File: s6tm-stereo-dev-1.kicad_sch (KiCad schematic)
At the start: 86 parts, among them J10 Conn_01x04_Pin, J2 Micro_SD_Card_Det1, J3 USB_C_Receptacle_USB2.0_14P, SW1 SW_SPDT, SW10 SW_Push, SW2 RotaryEncoder_Switch, SW5 SW_Push, SW6 SW_Push, SW7 SW_Push, SW9 SW_Push, U10 HS96L03W2C03, U4 ESP32-S3FN8, Y1 48M

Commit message: schem: add missing footprints
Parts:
- J2: footprint Pers:microSD_Hanbo_TF012 -> GLCS:microSD_Hanbo_TF012
- SW2: footprint RotaryEncoder_Alps_EC11E-Switch_Vertical_H20mm -> Rotary_Encoder:RotaryEncoder_Alps_EC11E-Switch_Vertical_H20mm
- U10: footprint Pers:HS96L03W2C03 -> GLCS:HS96L03W2C03
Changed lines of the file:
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@@
 			)
 		)
-		(property "Footprint" "Pers:microSD_Hanbo_TF012"
+		(property "Footprint" "GLCS:microSD_Hanbo_TF012"
 			(at 144.78 153.67 0)
 			(hide yes)
@@
 			)
 		)
-		(property "Footprint" "RotaryEncoder_Alps_EC11E-Switch_Vertical_H20mm"
+		(property "Footprint" "Rotary_Encoder:RotaryEncoder_Alps_EC11E-Switch_Vertical_H20mm"
 			(at 257.81 31.496 0)
 			(hide yes)
@@
 			)
 		)
-		(property "Footprint" "Pers:HS96L03W2C03"
+		(property "Footprint" "GLCS:HS96L03W2C03"
 			(at 260.35 55.245 0)
 			(hide yes)

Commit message: schem: run and fix ERC
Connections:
- net CHIP_PU: now also C14.1, R14.2, U4.4 (CHIP_PU/RESET)
- no-connect marks 9 -> 13
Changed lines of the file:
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@@
 	)
 	(junction
+		(at 254 153.67)
+		(diameter 0)
+		(color 0 0 0 0)
+	)
+	(junction
 		(at 195.58 119.38)
 		(diameter 0)
@@
 	)
 	(no_connect
+		(at 127 123.19)
+	)
+	(no_connect
 		(at 60.96 107.95)
 	)
 	(no_connect
+		(at 127 120.65)
+	)
+	(no_connect
 		(at 127 74.93)
 	)
 	(no_connect
+		(at 127 115.57)
+	)
+	(no_connect
 		(at 60.96 105.41)
 	)
@@
 	)
 	(no_connect
+		(at 127 118.11)
+	)
+	(no_connect
 		(at 60.96 102.87)
 	)
@@
 	(wire
 		(pts
-			(xy 251.46 153.67) (xy 255.27 153.67)
+			(xy 251.46 153.67) (xy 254 153.67)
 		)
 		(stroke
@@
 	(wire
 		(pts
+			(xy 254 153.67) (xy 255.27 153.67)
+		)
+		(stroke
+			(width 0)
+			(type default)
+		)
+	)
+	(wire
+		(pts
 			(xy 252.73 142.24) (xy 250.19 142.24)
 		)
@@
 		)
 	)
+	(label "CHIP_PU"
+		(at 59.69 64.77 180)
+		(effects
+			(font
+				(size 1.27 1.27)
+			)
+			(justify right bottom)
+		)
+	)
 	(label "DIN"
 		(at 134.62 85.09 180)
@@
 		(property "Value" "GND"
 			(at 60.706 189.738 0)
+			(hide yes)
 			(show_name no)
 			(do_not_autoplace no)
@@
 		(property "Value" "GND"
 			(at 45.212 189.738 0)
+			(hide yes)
 			(show_name no)
 			(do_not_autoplace no)
@@
 					(unit 1)
 				)
+			)
+		)
+	)
+	(symbol
+		(lib_id "power:PWR_FLAG")
+		(at 254 153.67 0)
+		(unit 1)
+		(body_style 1)
+		(exclude_from_sim no)
+		(in_bom yes)
+		(on_board yes)
+		(in_pos_files yes)
+		(dnp no)
+		(fields_autoplaced yes)
+		(property "Reference" "#FLG07"
+			(at 254 151.765 0)
+			(hide yes)
+			(show_name no)
+			(do_not_autoplace no)
+			(effects
+				(font
+					(size 1.27 1.27)
+				)
+			)
+		)
+		(property "Value" "PWR_FLAG"
+			(at 254 148.59 0)
+			(hide yes)
+			(show_name no)
+			(do_not_autoplace no)
+			(effects
+				(font
+					(size 1.27 1.27)
+				)
+			)
+		)
+		(property "Footprint" ""
+			(at 254 153.67 0)
+			(hide yes)
+			(show_name no)
+			(do_not_autoplace no)
+			(effects
+				(font
+					(size 1.27 1.27)
+				)
+			)
+		)
+		(property "Datasheet" ""
+			(at 254 153.67 0)
+			(hide yes)
+			(show_name no)
+			(do_not_autoplace no)
+			(effects
+				(font
+					(size 1.27 1.27)
+				)
+			)
+		)
+		(property "Description" "Special symbol for telling ERC where power comes from"
+			(at 254 153.67 0)
+			(hide yes)
+			(show_name no)
+			(do_not_autoplace no)
+			(effects
+				(font
+					(size 1.27 1.27)
+				)
+			)
+		)
+		(pin "1"
+		)
+		(instances
+			(project "s6tm-stereo-dev-1"
+				(path "/41fad0d7-0cae-453e-a16c-bdf8be036e99"
+					(reference "#FLG07")
+					(unit 1)
+				)

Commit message: schem: add title
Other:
- company: (none) -> Rémi Ait-Younes
- title: (none) -> S6TM Stereo Dev 1
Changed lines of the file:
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@@
 	(generator_version "10.0")
 	(paper "A4")
+	(title_block
+		(title "S6TM Stereo Dev 1")
+		(date "2026-04-11")
+		(rev "01")
+		(company "Rémi Ait-Younes")
+	)
 	(rectangle
 		(start 180.34 138.43)

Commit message: schem: reannotate
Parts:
- renumbered C12 to C1, C20 to C10, C21 to C11, C7 to C12, C8 to C13, C62 to C14, C4 to C2, C13 to C3, C14 to C4, C15 to C5, C16 to C6, C17 to C7, C18 to C8, C19 to C9, D17 to D1, D5 to D10, D12 to D2, D13 to D3, D14 to D4, D15 to D5, D1 to D6, D16 to D7, D2 to D8, D4 to D9, J2 to J1, J10 to J2, L2 to L1, L3 to L2, L4 to L3, L5 to L4, L1 to L5, R11 to R1, R47 to R10, R48 to R11, R49 to R12, R43 to R13, R42 to R14, R16 to R15, R17 to R16, R41 to R17, R14 to R2, R40 to R20, R38 to R21, R39 to R22, R32 to R23, R33 to R24, R34 to R25, R1 to R26, R2 to R27, R35 to R28, R36 to R29, R61 to R3, R37 to R30, R52 to R4, R51 to R5, R50 to R6, R44 to R7, R45 to R8, R46 to R9, SW5 to SW2, SW6 to SW3, SW7 to SW4, SW9 to SW5, SW10 to SW6, SW2 to SW7, TP20 to TP1, TP8 to TP12, TP19 to TP2, TP18 to TP3, TP17 to TP4, TP16 to TP5, TP15 to TP6, TP14 to TP7, TP13 to TP8, TP12 to TP9, U4 to U1, U10 to U2

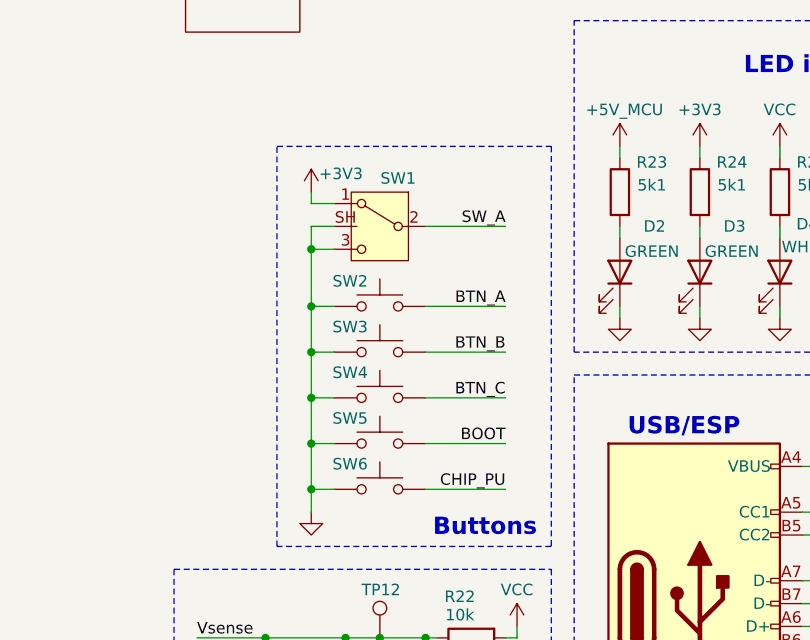
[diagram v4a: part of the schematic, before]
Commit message: schem: remove BTN_C
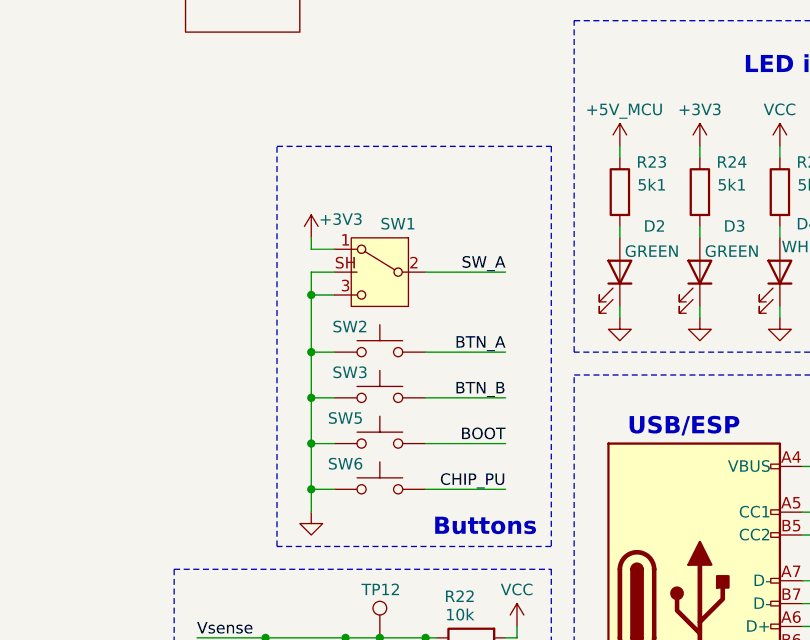
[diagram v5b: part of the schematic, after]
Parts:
- removed SW4: SW_Push, Button_Switch_THT:SW_SPST_Omron_B3F-40xx, symbol Switch:SW_Push
- SW5, SW6: footprint Button_Switch_THT:SW_SPST_Omron_B3F-40xx -> Button_Switch_SMD:SW_SPST_TS-1088-xR020; Basic Z -> Y; JLCPCB Part # C84931 -> C720477; Manufacturer OMRON -> XUNPU; Manufacturer Part Number B3F-4055 -> TS-1088-AR02016
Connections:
- net BOOT: now also SW5.2; no longer SW5.1
- net CHIP_PU: now also SW6.2; no longer SW6.1
- net GND: now also SW5.1, SW6.1; no longer SW5.2, SW6.2
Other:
- moved on the sheet: SW1, SW2, SW3

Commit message: schem: update esp32s3 footprint
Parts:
- U1: footprint Package_DFN_QFN:QFN-56-1EP_7x7mm_P0.4mm_EP5.6x5.6mm -> Package_DFN_QFN:QFN-56-1EP_7x7mm_P0.4mm_EP4x4mm_ThermalVias
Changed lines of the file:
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@@
 			)
 		)
-		(property "Footprint" "Package_DFN_QFN:QFN-56-1EP_7x7mm_P0.4mm_EP5.6x5.6mm"
+		(property "Footprint" "Package_DFN_QFN:QFN-56-1EP_7x7mm_P0.4mm_EP4x4mm_ThermalVias"
 			(at 93.98 140.97 0)
 			(hide yes)

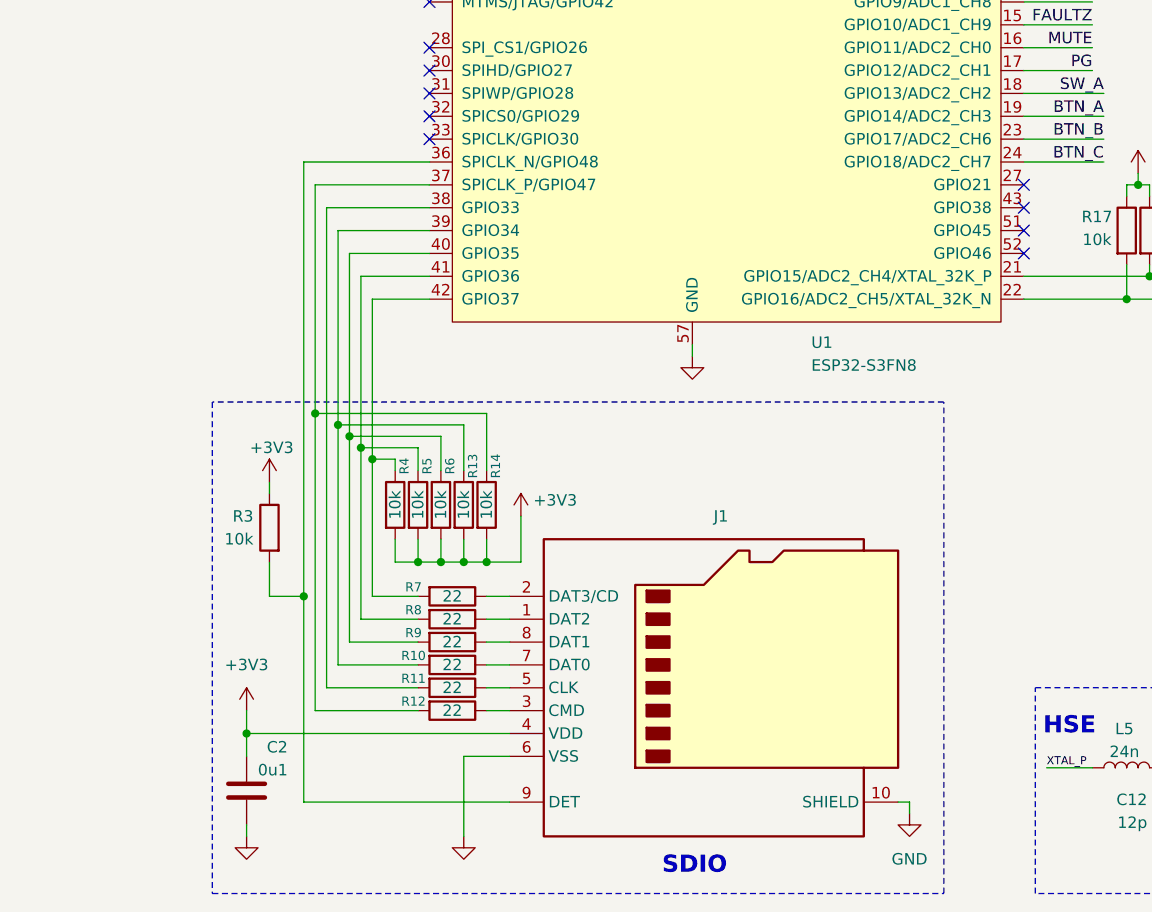
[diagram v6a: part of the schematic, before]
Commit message: schem: add M3 mounting holes
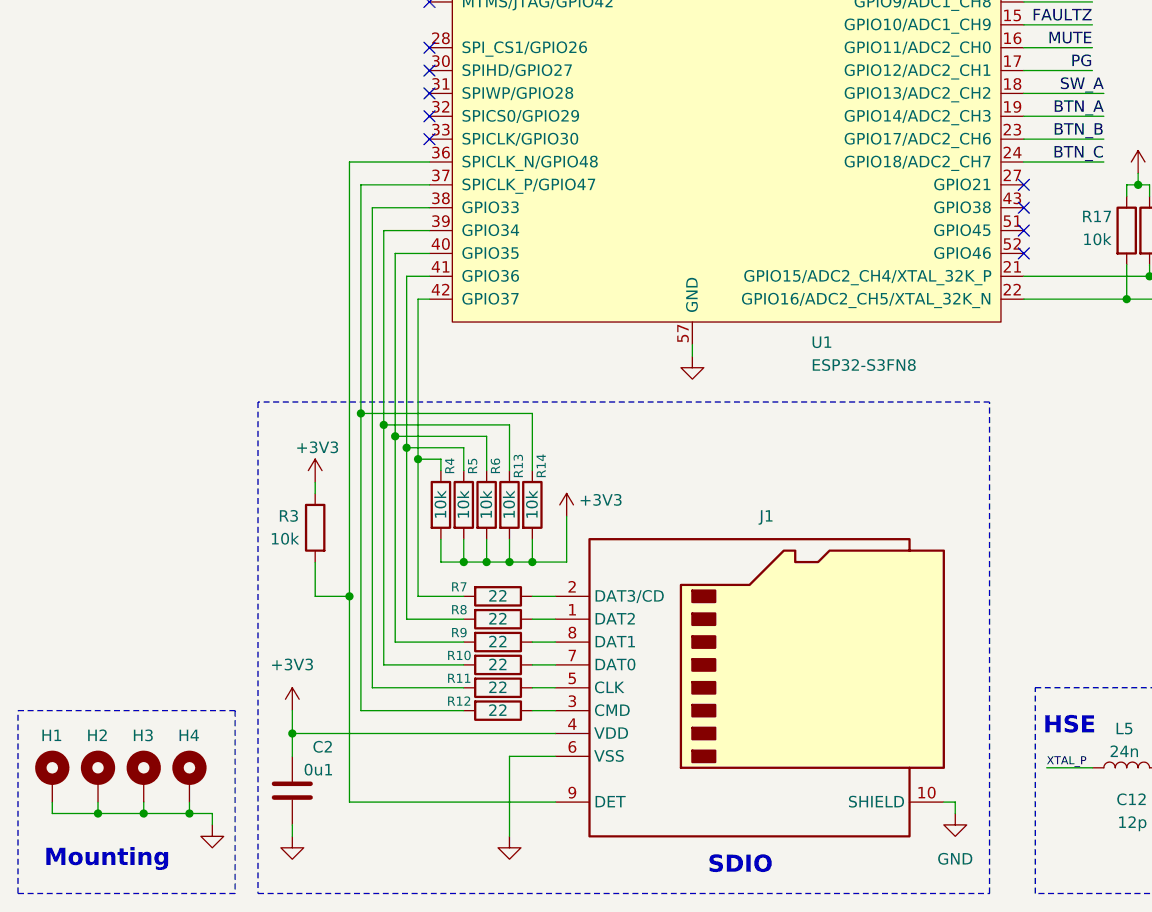
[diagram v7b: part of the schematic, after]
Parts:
- added H1, H2, H3, H4: MountingHole_Pad, MountingHole:MountingHole_3.2mm_M3_Pad_Via, symbol Mechanical:MountingHole_Pad
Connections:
- net GND: now also H1.1, H2.1, H3.1, H4.1
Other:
- note added: "Mounting"
- moved on the sheet: C2, J1, R10, R11, R12, R13, R14, R3, R4, R5, R6, R7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

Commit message: schem/pcb: add smt fiducials and tooling holes
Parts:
- added FID1, FID2, FID3: Fiducial, Fiducial:Fiducial_1mm_Mask2mm, symbol Mechanical:Fiducial
- added H5, H6, H7: MountingHole, MountingHole:ToolingHole_1.152mm, symbol Mechanical:MountingHole
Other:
- note added: "SMT assembly"
